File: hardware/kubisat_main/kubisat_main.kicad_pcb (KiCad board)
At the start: 2 copper layers, 80 x 80 mm, 1 part, among them U1 ATSAMD21G18A-A

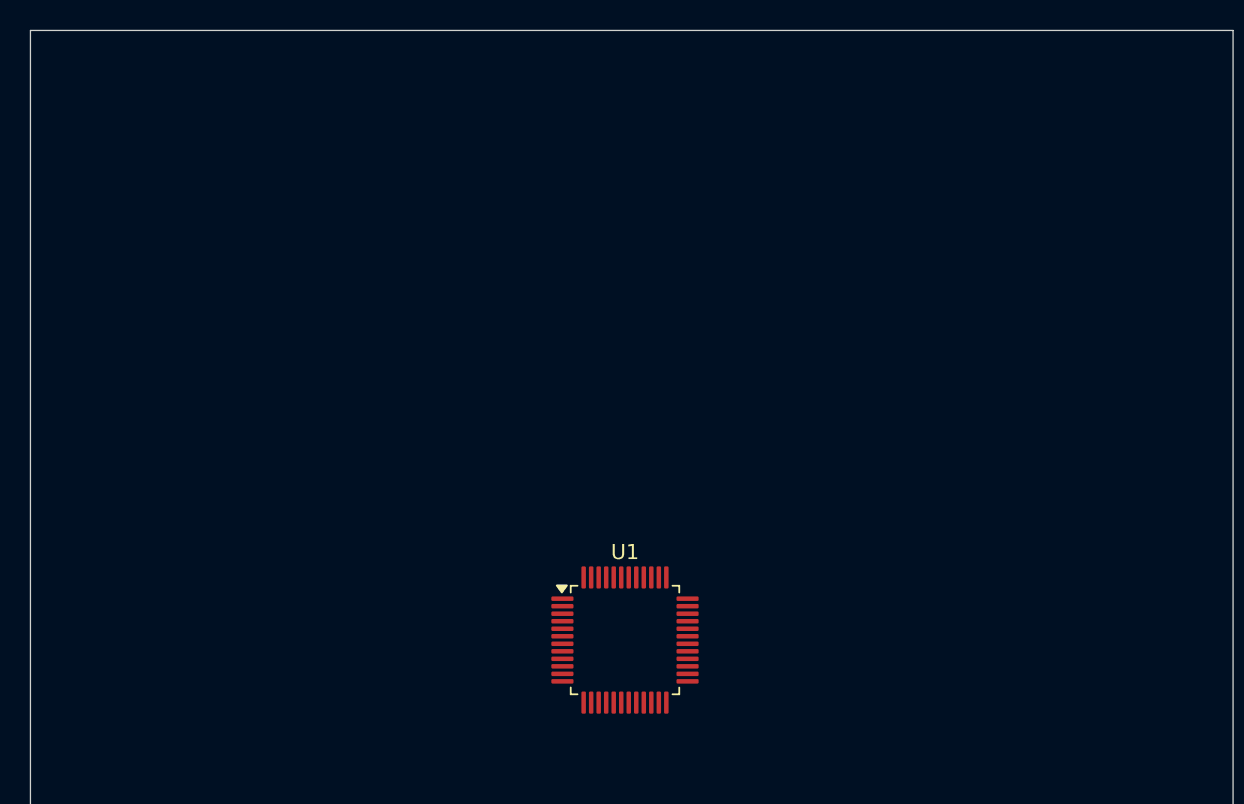
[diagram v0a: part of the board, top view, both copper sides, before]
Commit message: added arduino code, more items on main schematic
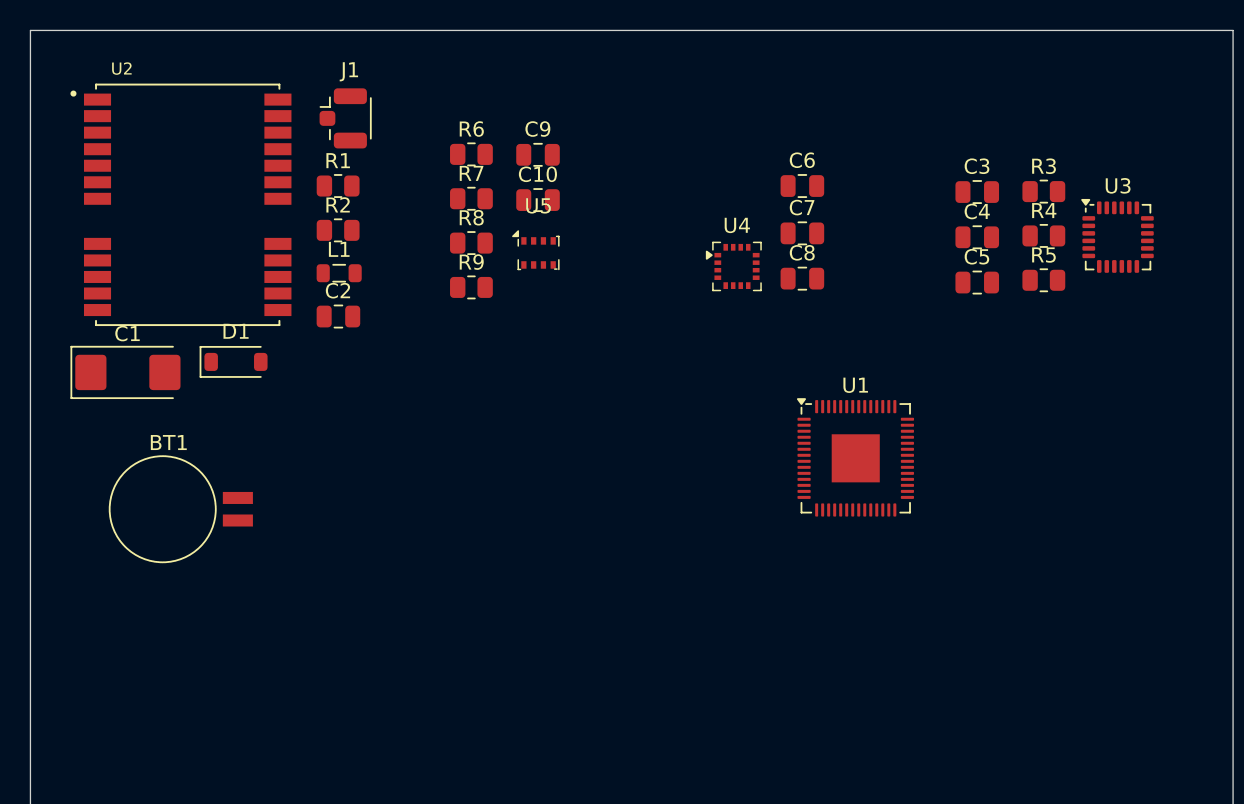
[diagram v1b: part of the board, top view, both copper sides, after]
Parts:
- added BT1: Battery_Cell, Battery:BatteryHolder_Seiko_MS621F, F.Cu at (43.8, 66.8)
- added C1: 220u/10V, Capacitor_Tantalum_SMD:CP_EIA-6032-15_Kemet-U, F.Cu at (36.5, 57.8)
- added C10: 1u, Capacitor_SMD:C_0805_2012Metric, F.Cu at (63.8, 46.3)
- added C2: 100n, Capacitor_SMD:C_0805_2012Metric, F.Cu at (50.5, 54.0)
- added C3: 100n, Capacitor_SMD:C_0805_2012Metric, F.Cu at (93.0, 45.8)
- added C4: 10n, Capacitor_SMD:C_0805_2012Metric, F.Cu at (93.0, 48.8)
- added C5: 2n2, Capacitor_SMD:C_0805_2012Metric, F.Cu at (93.0, 51.8)
- added C6: 100n, Capacitor_SMD:C_0805_2012Metric, F.Cu at (81.3, 45.4)
- added C7: 4u7, Capacitor_SMD:C_0805_2012Metric, F.Cu at (81.3, 48.5)
- added C8: 200n, Capacitor_SMD:C_0805_2012Metric, F.Cu at (81.3, 51.5)
- added C9: 100n, Capacitor_SMD:C_0805_2012Metric, F.Cu at (63.8, 43.3)
- added D1: 1N5817, Diode_SMD:D_SOD-123, F.Cu at (43.7, 57.0)
- added J1: IPX, Connector_Coaxial:U.FL_Hirose_U.FL-R-SMT-1_Vertical, F.Cu at (50.8, 40.9)
- added L1: 27uH, Inductor_SMD:L_0805_2012Metric, F.Cu at (50.5, 51.1)
- added R1: 22, Resistor_SMD:R_0805_2012Metric, F.Cu at (50.5, 45.4)
- added R2: 1k, Resistor_SMD:R_0805_2012Metric, F.Cu at (50.5, 48.3)
- added R3: 4k7, Resistor_SMD:R_0805_2012Metric, F.Cu at (97.4, 45.7)
- added R4: 4k7, Resistor_SMD:R_0805_2012Metric, F.Cu at (97.4, 48.7)
- added R5: 4k7, Resistor_SMD:R_0805_2012Metric, F.Cu at (97.4, 51.6)
- added R6: 10k, Resistor_SMD:R_0805_2012Metric, F.Cu at (59.3, 43.2)
- added R7: 10k, Resistor_SMD:R_0805_2012Metric, F.Cu at (59.3, 46.2)
- added R8: 10k, Resistor_SMD:R_0805_2012Metric, F.Cu at (59.3, 49.1)
- added R9: 10k, Resistor_SMD:R_0805_2012Metric, F.Cu at (59.3, 52.1)
- added U2: NEO-6M-GPS, RF_GPS:XCVR_NEO-6M-GPS, F.Cu at (40.5, 46.6)
- added U3: MPU-6050, Sensor_Motion:InvenSense_QFN-24_4x4mm_P0.5mm, F.Cu at (102.3, 48.8)
- added U4: MMC5883MA, Package_LGA:LGA-16_3x3mm_P0.5mm, F.Cu at (77.0, 50.7)
- added U5: BMP280, Package_LGA:Bosch_LGA-8_2x2.5mm_P0.65mm_ClockwisePinNumbering, F.Cu at (63.8, 49.8)
- U1: value ATSAMD21G18A-A -> RP2040; footprint Package_QFP:TQFP-48_7x7mm_P0.5mm -> Package_DFN_QFN:QFN-56-1EP_7x7mm_P0.4mm_EP3.2x3.2mm
- moved U1 19.5 mm to (84.9, 63.5)
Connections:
- U1 pad 1: unconnected-(U1-PA00-Pad1) -> Net-(U1-IOVDD-Pad1)
- U1 pad 10: unconnected-(U1-PA05-Pad10) -> Net-(U1-IOVDD-Pad1)
- U1 pad 18: Net-(U1-GND-Pad18) -> unconnected-(U1-GPIO15-Pad18)
- U1 pad 22: unconnected-(U1-PA13-Pad22) -> Net-(U1-IOVDD-Pad1)
- U1 pad 23: unconnected-(U1-PA14-Pad23) -> Net-(U1-DVDD-Pad23)
- U1 pad 33: unconnected-(U1-PA24-Pad33) -> Net-(U1-IOVDD-Pad1)
- U1 pad 35: Net-(U1-GND-Pad18) -> unconnected-(U1-GPIO23-Pad35)
- U1 pad 42: Net-(U1-GND-Pad18) -> Net-(U1-IOVDD-Pad1)

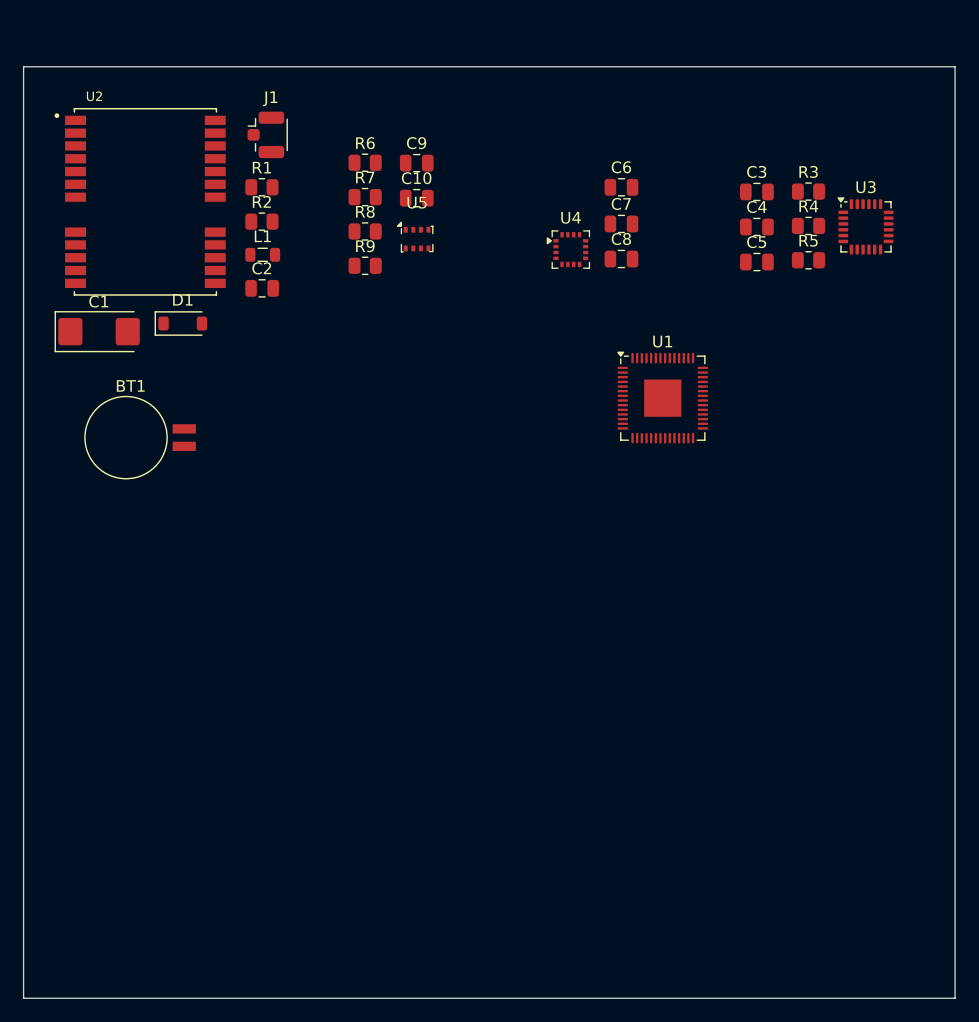
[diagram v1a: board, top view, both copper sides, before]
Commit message: added elements and traces to main pcb
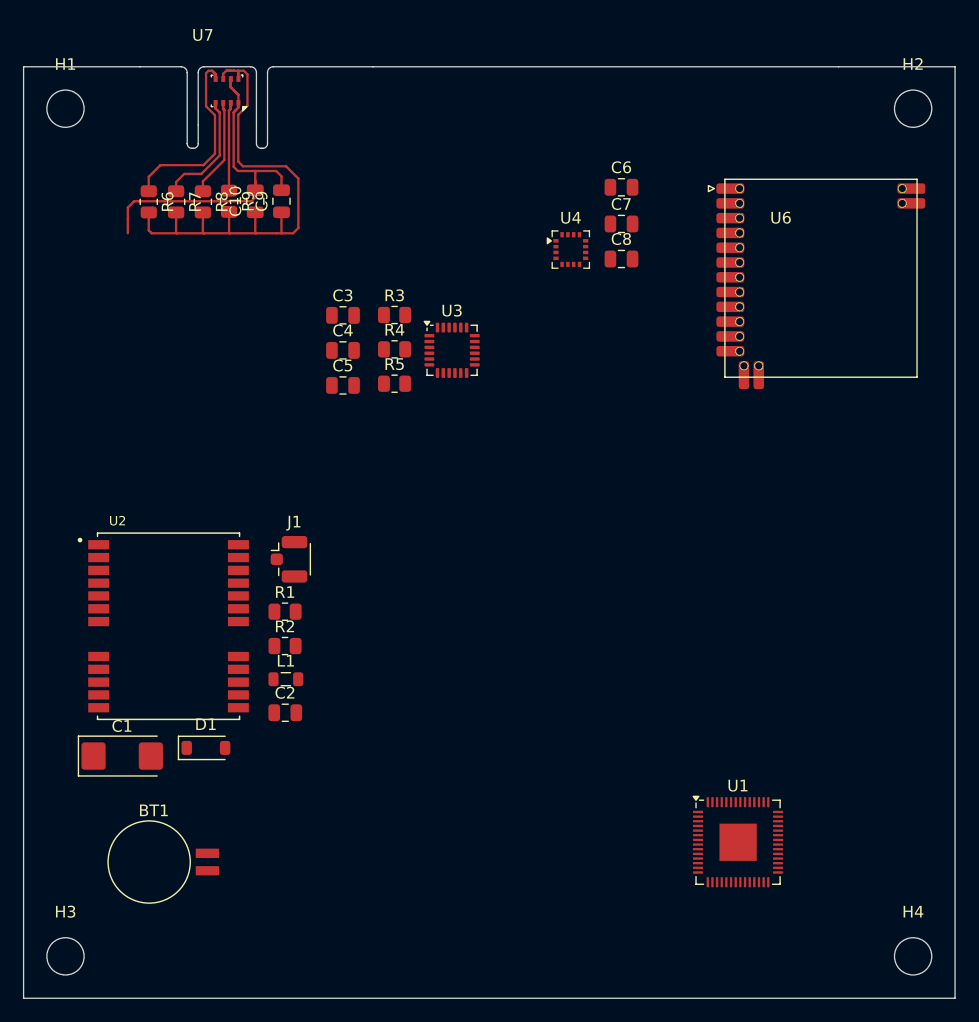
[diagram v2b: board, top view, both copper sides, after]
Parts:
- removed U5: BMP280, Package_LGA:Bosch_LGA-8_2x2.5mm_P0.65mm_ClockwisePinNumbering
- added H1: MountingHole, MountingHole:MountingHole_3.2mm_M3_DIN965, F.Cu at (33.6, 38.6)
- added H2: MountingHole, MountingHole:MountingHole_3.2mm_M3_DIN965, F.Cu at (106.4, 38.6)
- added H3: MountingHole, MountingHole:MountingHole_3.2mm_M3_DIN965, F.Cu at (33.6, 111.4)
- added H4: MountingHole, MountingHole:MountingHole_3.2mm_M3_DIN965, F.Cu at (106.4, 111.4)
- added U6: XL1278-SMT, RF:XL1278-SMT, F.Cu at (91.5, 45.5)
- added U7: BME280, Package_LGA:Bosch_LGA-8_2.5x2.5mm_P0.65mm_ClockwisePinNumbering, F.Cu at (47.5, 37.1)
- moved U1 38.7 mm to (91.4, 101.6)
- moved C3 37.1 mm to (57.4, 56.4)
- moved C4 37.1 mm to (57.4, 59.4)
- moved C5 37.1 mm to (57.4, 62.4)
- moved R3 37.1 mm to (61.9, 56.3)
- moved R4 37.1 mm to (61.9, 59.3)
- moved R5 37.1 mm to (61.9, 62.2)
- moved U3 37.1 mm to (66.8, 59.4)
- moved BT1 36.5 mm to (45.8, 103.3)
- moved C1 36.5 mm to (38.5, 94.2)
- moved C2 36.5 mm to (52.5, 90.5)
- moved D1 36.5 mm to (45.7, 93.5)
- moved R2 36.5 mm to (52.5, 84.8)
- moved J1 36.5 mm to (52.8, 77.3)
- moved L1 36.5 mm to (52.5, 87.6)
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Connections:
- C7 pad 1: Net-(U4-CAP) -> unconnected-(C7-Pad1)
- C8 pad 1: Net-(U4-SETP) -> unconnected-(C8-Pad1)
- C8 pad 2: Net-(U4-SETC) -> unconnected-(C8-Pad2)
- R6 pad 1: SCL -> Net-(U7-SDO)
- R7 pad 1: SDA -> SCL
- R8 pad 1: Net-(U5-SDO) -> SDA
- U3 pad 6: Net-(U3-AUX_DA) -> unconnected-(U3-AUX_DA-Pad6)
- U3 pad 7: Net-(U3-AUX_CL) -> unconnected-(U3-AUX_CL-Pad7)
- U4 pad 1: Net-(U3-AUX_CL) -> unconnected-(U4-SCL-Pad1)
- U4 pad 10: Net-(U4-CAP) -> unconnected-(U4-CAP-Pad10)
- U4 pad 11: GND -> Net-(U4-GND-Pad11)
- U4 pad 12: Net-(U4-SETC) -> unconnected-(U4-NC-Pad12)
- U4 pad 13: +3V3 -> unconnected-(U4-VDDIO-Pad13)
- U4 pad 15: MDRDY -> unconnected-(U4-INT-Pad15)
- U4 pad 16: Net-(U3-AUX_DA) -> unconnected-(U4-SDA-Pad16)
- U4 pad 2: +3V3 -> unconnected-(U4-VDD-Pad2)
- U4 pad 4: +3V3 -> unconnected-(U4-NC-Pad4)
- U4 pad 8: Net-(U4-SETP) -> unconnected-(U4-NC-Pad8)
- U4 pad 9: GND -> Net-(U4-GND-Pad11)
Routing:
- net +3V3: track 0.00 -> 46.8 mm
- net GND: track 0.00 -> 32.8 mm
- net Net-(U7-SDO): track 0.00 -> 17.3 mm
- net SCL: track 0.00 -> 11.2 mm
- net SDA: track 0.00 -> 9.11 mm
- net Net-(U7-CSB): track 0.00 -> 8.39 mm
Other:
- outline, holes or cut-outs redrawn

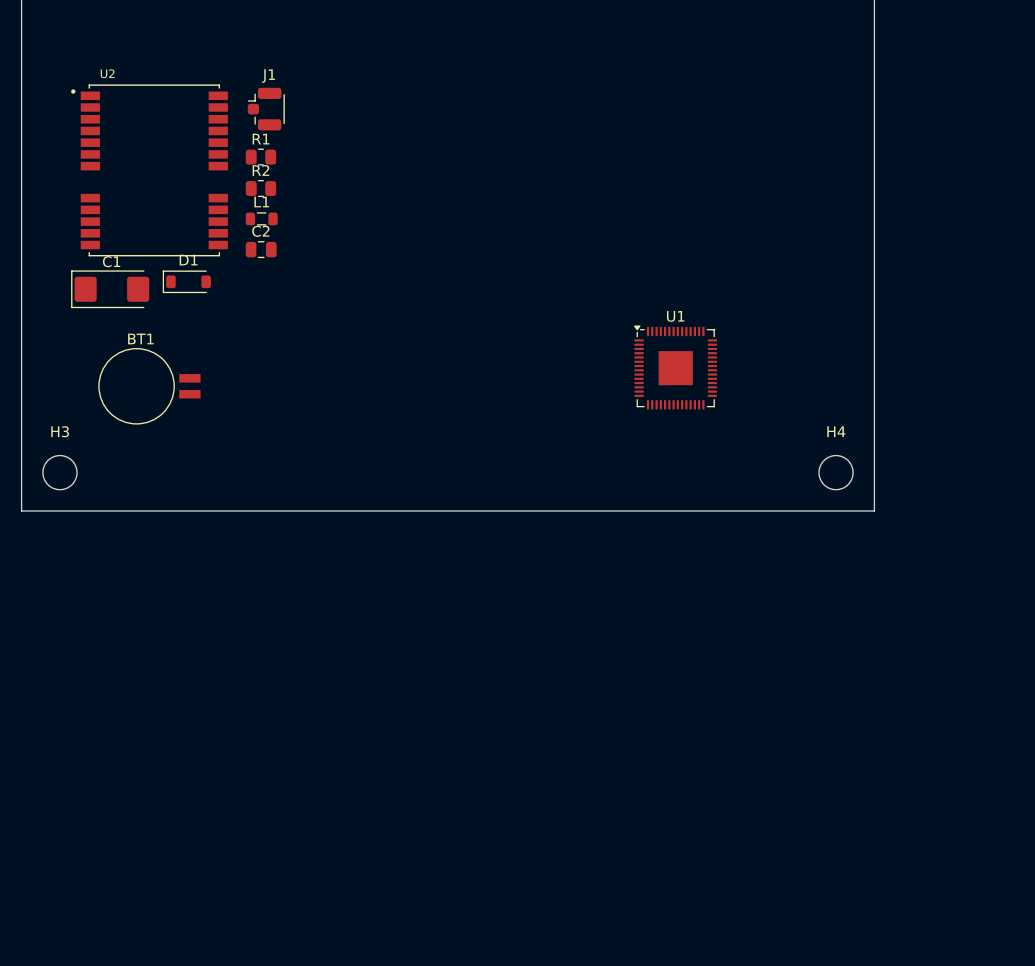
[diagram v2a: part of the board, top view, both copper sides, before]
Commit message: added microsd footprint
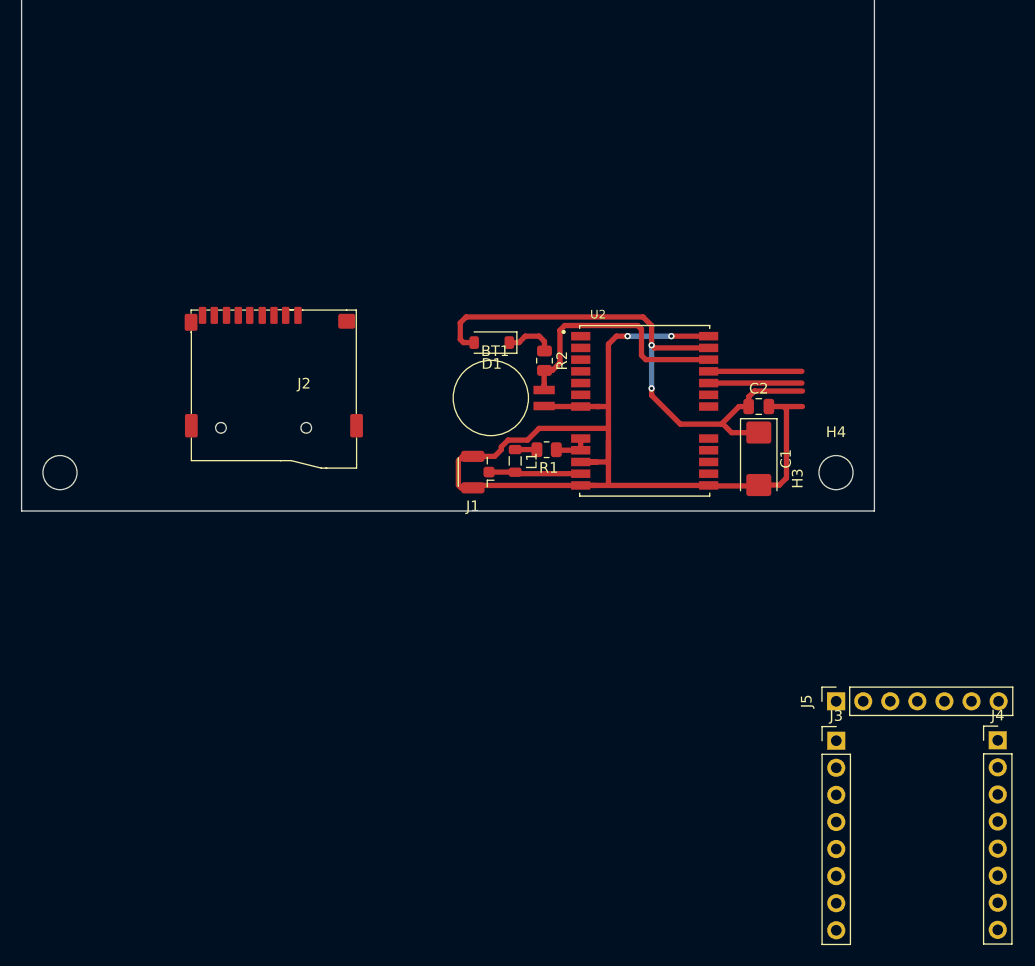
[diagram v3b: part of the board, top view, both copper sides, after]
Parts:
- removed U1: RP2040, Package_DFN_QFN:QFN-56-1EP_7x7mm_P0.4mm_EP3.2x3.2mm
- added J2: Micro_SD_Card_Det1, Connector_Card:MR01A-01211, F.Cu at (56.5, 103.0)
- added J3: Conn_01x08_Socket, Connector_PinHeader_2.54mm:PinHeader_1x08_P2.54mm_Vertical, F.Cu at (106.4, 136.6)
- added J4: Conn_01x08_Socket, Connector_PinHeader_2.54mm:PinHeader_1x08_P2.54mm_Vertical, F.Cu at (121.6, 136.5)
- added J5: Conn_01x07_Socket, Connector_PinSocket_2.54mm:PinSocket_1x07_P2.54mm_Vertical, F.Cu at (106.4, 132.8)
- moved C1 62.7 mm to (99.2, 110.1), turned to -90 degrees
- moved U2 51.2 mm to (88.5, 105.6)
- moved C2 48.9 mm to (99.2, 105.2)
- moved J1 39.5 mm to (72.8, 111.3), turned to 180 degrees
- moved R1 38.4 mm to (79.2, 109.2), turned to 180 degrees
- moved BT1 33.2 mm to (79.0, 104.4)
- moved L1 32.9 mm to (76.3, 110.3), turned to -90 degrees
- moved R2 31.1 mm to (79.0, 100.9), turned to -90 degrees
- moved D1 29.0 mm to (74.1, 99.2), turned to 180 degrees
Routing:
- net GND: track 32.8 -> 128.3 mm, vias 0 -> 2
- net +3V3: track 46.8 -> 101.4 mm, vias 0 -> 2
- net Net-(BT1-+): track 0.00 -> 23.6 mm
- net unconnected-(U2-TXD1-Pad20): track 0.00 -> 8.75 mm
- net unconnected-(U2-RXD1-Pad21): track 0.00 -> 8.75 mm
- net RF_IN: track 0.00 -> 8.66 mm
- net Net-(D1-K): track 0.00 -> 4.64 mm
- net Net-(U2-RSVD_8): track 0.00 -> 3.15 mm
- net Net-(L1-Pad1): track 0.00 -> 2.04 mm

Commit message: added elements to cpu schematic
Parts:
- removed J4: Conn_01x08_Socket, Connector_PinHeader_2.54mm:PinHeader_1x08_P2.54mm_Vertical
- removed J5: Conn_01x07_Socket, Connector_PinSocket_2.54mm:PinSocket_1x07_P2.54mm_Vertical
- added C11: 100n, Capacitor_SMD:C_0805_2012Metric, F.Cu at (114.9, 70.8)
- added C12: 100n, Capacitor_SMD:C_0805_2012Metric, F.Cu at (114.9, 73.8)
- added C13: 2u2, Capacitor_SMD:C_0805_2012Metric, F.Cu at (114.9, 76.8)
- added C14: 100n, Capacitor_SMD:C_0805_2012Metric, F.Cu at (114.9, 79.8)
- added C15: 2u2, Capacitor_SMD:C_0805_2012Metric, F.Cu at (114.9, 82.9)
- added C16: 15p, Capacitor_SMD:C_0805_2012Metric, F.Cu at (114.9, 85.9)
- added C17: 15p, Capacitor_SMD:C_0805_2012Metric, F.Cu at (114.9, 88.9)
- added C18: 100n, Capacitor_SMD:C_0805_2012Metric, F.Cu at (143.8, 70.2)
- added C19: 100n, Capacitor_SMD:C_0805_2012Metric, F.Cu at (143.8, 73.2)
- added C20: 100n, Capacitor_SMD:C_0805_2012Metric, F.Cu at (143.8, 76.2)
- added C21: 100n, Capacitor_SMD:C_0805_2012Metric, F.Cu at (143.8, 79.3)
- added C22: 100n, Capacitor_SMD:C_0805_2012Metric, F.Cu at (143.8, 82.3)
- added C23: 100n, Capacitor_SMD:C_0805_2012Metric, F.Cu at (143.8, 85.3)
- added C24: 100n, Capacitor_SMD:C_0805_2012Metric, F.Cu at (143.8, 88.3)
- added C25: 100n, Capacitor_SMD:C_0805_2012Metric, F.Cu at (143.8, 91.3)
- added SW1: BOOTSEL, Button_Switch_SMD:SW_MEC_5GSH9, F.Cu at (123.0, 77.6)
- added SW2: RESET, Button_Switch_SMD:SW_MEC_5GSH9, F.Cu at (151.8, 88.3)
- added U1: RP2040, Package_DFN_QFN:QFN-56-1EP_7x7mm_P0.4mm_EP3.2x3.2mm, F.Cu at (133.4, 74.0)
- added U6: W25Q16JVSS, Package_SO:SOIC-8_5.23x5.23mm_P1.27mm, F.Cu at (122.3, 89.3)
- added U8: DS3231M, Package_SO:SOIC-16W_7.5x10.3mm_P1.27mm, F.Cu at (172.7, 74.8)
- added Y1: 12MHz, Crystal:Crystal_SMD_3225-4Pin_3.2x2.5mm, F.Cu at (131.4, 80.8)
- J3: value Conn_01x08_Socket -> Conn_01x06_MountingPin; footprint Connector_PinHeader_2.54mm:PinHeader_1x08_P2.54mm_Vertical -> Connector_JST:JST_PH_S6B-PH-SM4-TB_1x06-1MP_P2.00mm_Horizontal
- moved J3 79.0 mm to (155.1, 74.3)
